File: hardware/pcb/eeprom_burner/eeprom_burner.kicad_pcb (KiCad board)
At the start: 2 copper layers, 68.6 x 53.3 mm, 17 parts, among them J1 Conn_01x08, J2 Conn_01x08, J4 Conn_01x06, P1 Power, P2 Analog, P3 Digital, P4 Digital, P5 CONN_01X01, P6 CONN_01X01, P7 CONN_01X01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

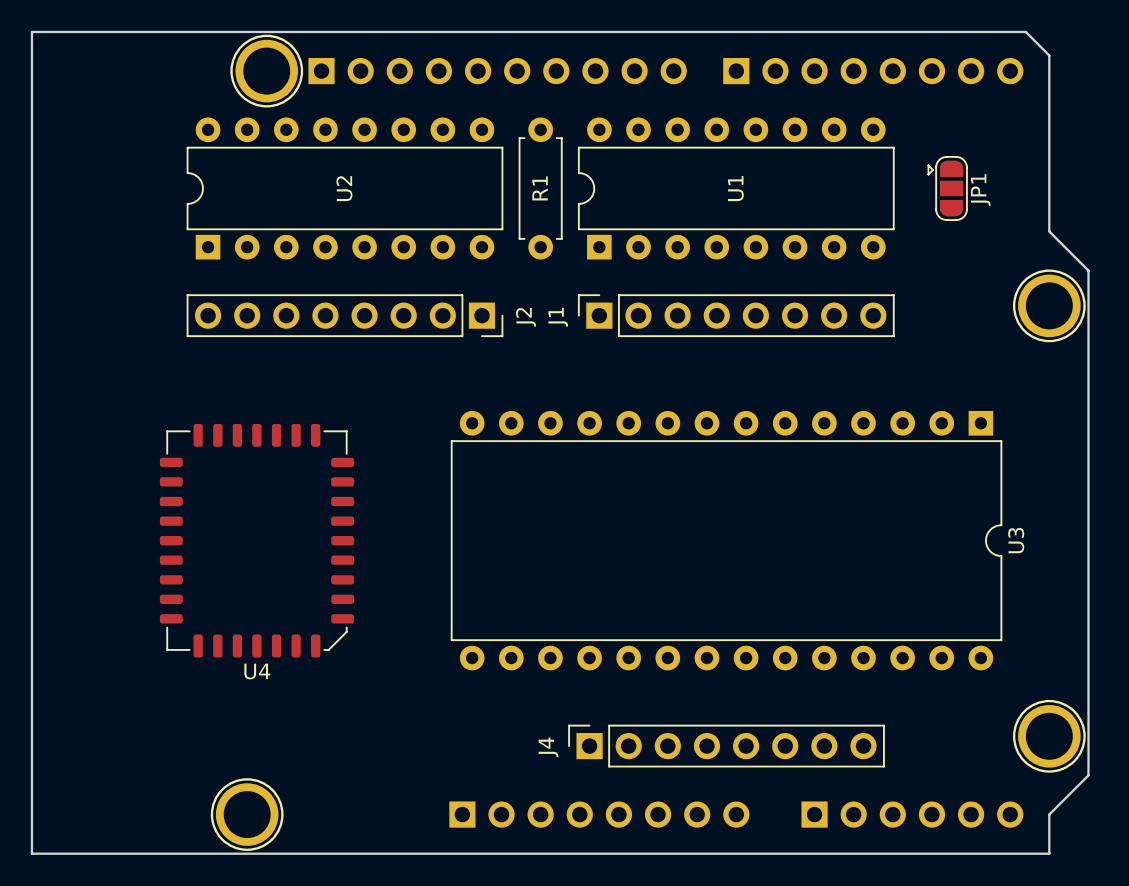
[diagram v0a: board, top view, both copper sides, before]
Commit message: Add decoupling capacitors
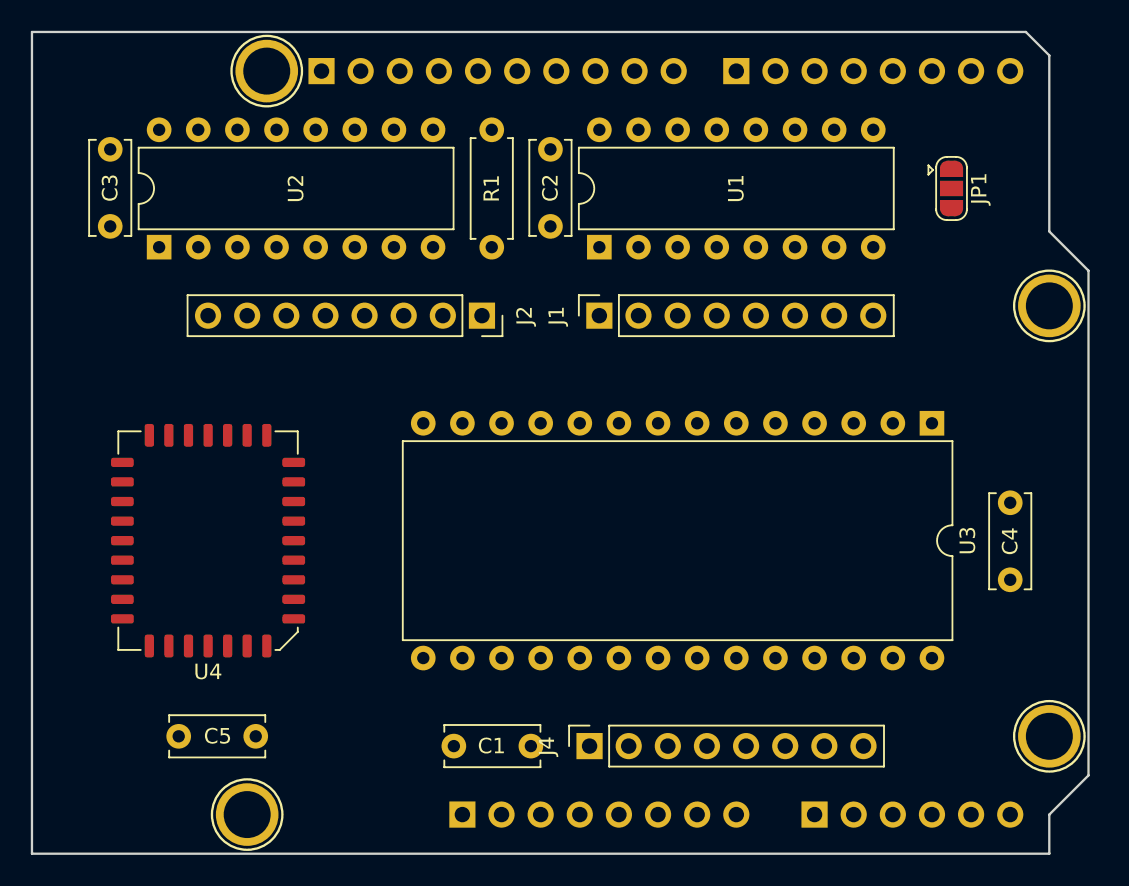
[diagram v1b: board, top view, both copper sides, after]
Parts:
- added C1: 100nF, Capacitor_THT:C_Disc_D6.0mm_W2.5mm_P5.00mm, F.Cu at (143.4, 119.4)
- added C2: 100nF, Capacitor_THT:C_Disc_D6.0mm_W2.5mm_P5.00mm, F.Cu at (144.7, 80.6)
- added C3: 100nF, Capacitor_THT:C_Disc_D6.0mm_W2.5mm_P5.00mm, F.Cu at (116.1, 80.6)
- added C4: 100nF, Capacitor_THT:C_Disc_D6.0mm_W2.5mm_P5.00mm, F.Cu at (174.5, 108.6)
- added C5: 100nF, Capacitor_THT:C_Disc_D6.0mm_W2.5mm_P5.00mm, F.Cu at (120.5, 118.7)
- moved R1 3.18 mm to (140.8, 79.4)
- moved U2 3.17 mm to (119.3, 87.0)
- moved U4 3.17 mm to (122.4, 106.0)
- moved U3 3.17 mm to (169.4, 98.4)

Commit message: Reorder for convinient address access
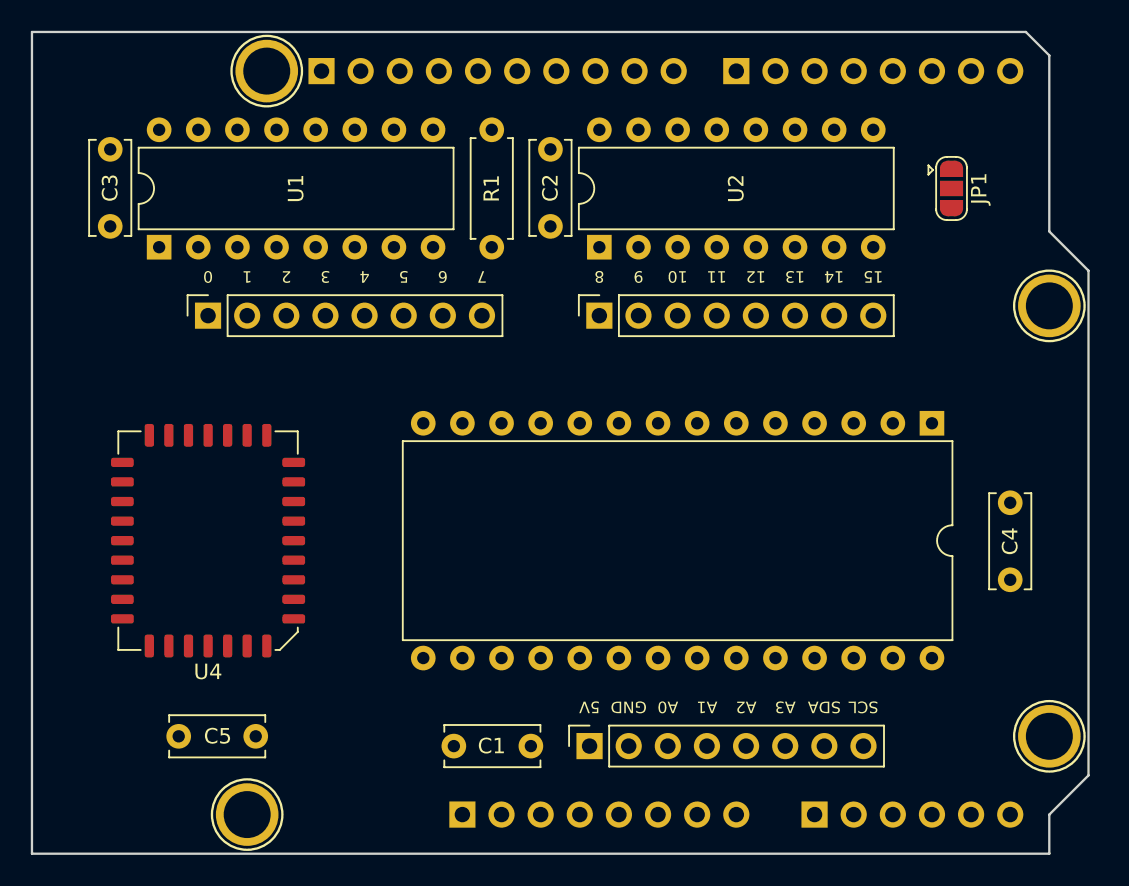
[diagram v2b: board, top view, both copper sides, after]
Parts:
- moved U1 28.6 mm to (119.3, 87.0)
- moved U2 28.6 mm to (147.8, 87.0)
- moved J1 25.4 mm to (122.4, 91.4)
- moved J2 7.62 mm to (147.8, 91.4), turned to 90 degrees
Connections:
- J2 pad 1: A15 -> A8
- J2 pad 2: A14 -> A9
- J2 pad 3: A13 -> A10
- J2 pad 4: A12 -> A11
- J2 pad 5: A11 -> A12
- J2 pad 6: A10 -> A13
- J2 pad 7: A9 -> A14
- J2 pad 8: A8 -> A15
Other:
- board text added: "0"
- board text added: "1"
- board text added: "10"
- board text added: "11"
- board text added: "12"
- board text added: "13"
- board text added: "14"
- board text added: "15"
- board text added: "2"
- board text added: "3"
- board text added: "4"
- board text added: "5"
- board text added: "5V"
- board text added: "6"
- board text added: "7"
- board text added: "8"
- board text added: "9"
- board text added: "A0"
- board text added: "A1"
- board text added: "A2"
- board text added: "A3"
- board text added: "GND"
- board text added: "SCL"
- board text added: "SDA"

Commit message: Add bus connector
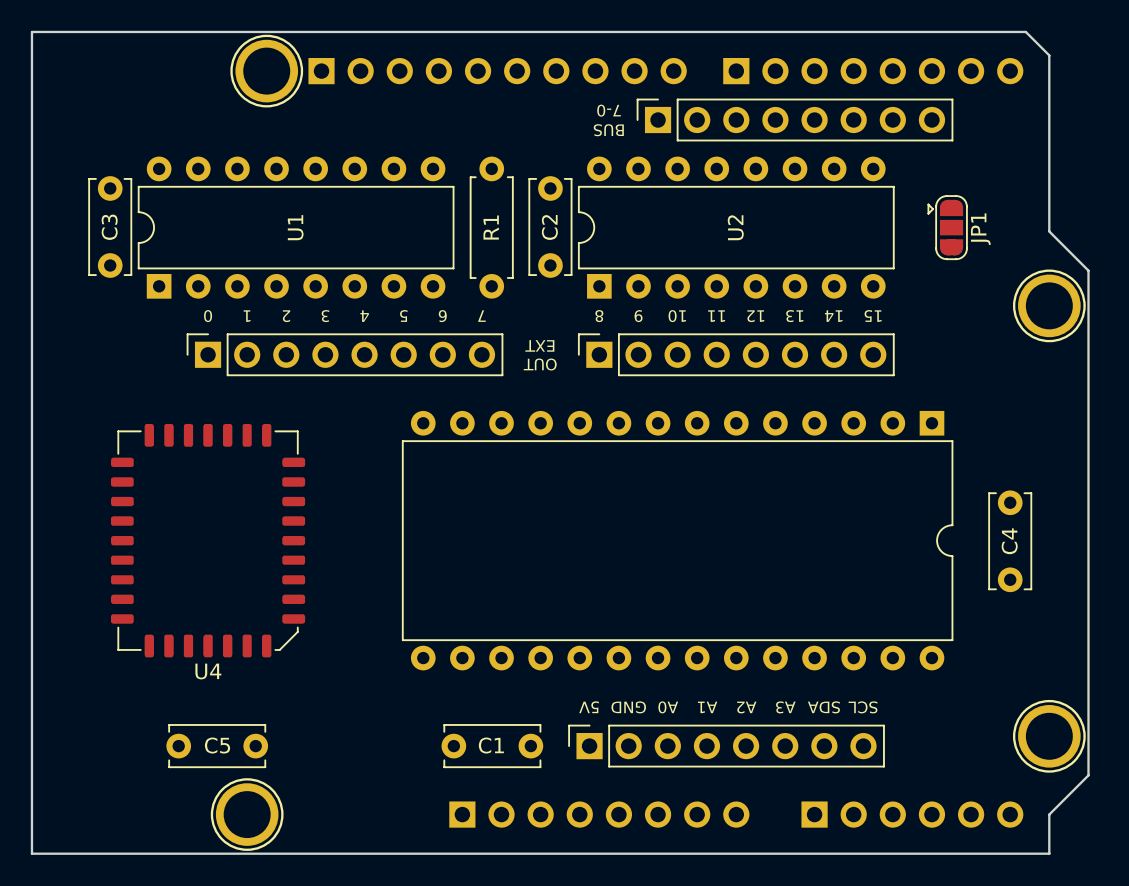
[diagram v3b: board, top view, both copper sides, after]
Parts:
- added J3: Conn_01x08, Connector_PinSocket_2.54mm:PinSocket_1x08_P2.54mm_Vertical, F.Cu at (151.6, 78.7)
- moved C2 2.54 mm to (144.7, 83.2)
- moved C3 2.54 mm to (116.1, 83.2)
- moved J1 2.54 mm to (122.4, 94.0)
- moved J2 2.54 mm to (147.8, 94.0)
- moved R1 2.54 mm to (140.8, 81.9)
- moved JP1 2.54 mm to (170.7, 85.7)
- moved U1 2.54 mm to (119.3, 89.5)
- moved U2 2.54 mm to (147.8, 89.5)
- moved C5 0.63 mm to (120.5, 119.4)
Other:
- board text added: "7-0"
- board text added: "BUS"
- board text added: "OUT EXT"

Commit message: Signature
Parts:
- moved C5 6.35 mm to (126.9, 119.4)
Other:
- board text added: "(c) Velko 2020"
- board text added: "EEPROM writer"
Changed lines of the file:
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@@
   (general
     (thickness 1.6)
-    (drawings 53)
+    (drawings 55)
     (tracks 0)
     (zones 0)
@@
     (descr "Through hole straight pin header, 1x06, 2.54mm pitch, single row")
     (tags "Through hole pin header THT 1x06 2.54mm single row")
-    (fp_text reference P2 (at -2.54 -6.35) (layer B.SilkS)
+    (fp_text reference P2 (at -2.54 -6.35) (layer B.SilkS) hide
       (effects (font (size 1 1) (thickness 0.15)) (justify mirror))
     )
@@
     (descr "Through hole straight pin header, 1x08, 2.54mm pitch, single row")
     (tags "Through hole pin header THT 1x08 2.54mm single row")
-    (fp_text reference P1 (at -2.54 -8.89) (layer B.SilkS)
+    (fp_text reference P1 (at -2.54 -8.89) (layer B.SilkS) hide
       (effects (font (size 1 1) (thickness 0.15)) (justify mirror))
     )
@@
     (descr "Through hole straight pin header, 1x08, 2.54mm pitch, single row")
     (tags "Through hole pin header THT 1x08 2.54mm single row")
-    (fp_text reference P4 (at 2.54 -9.525 180) (layer B.SilkS)
+    (fp_text reference P4 (at 2.54 -9.525 180) (layer B.SilkS) hide
       (effects (font (size 1 1) (thickness 0.15)) (justify mirror))
     )
@@
     (descr "Through hole straight pin header, 1x10, 2.54mm pitch, single row")
     (tags "Through hole pin header THT 1x10 2.54mm single row")
-    (fp_text reference P3 (at 2.54 -12.319 180) (layer B.SilkS)
+    (fp_text reference P3 (at 2.54 -12.319 180) (layer B.SilkS) hide
       (effects (font (size 1 1) (thickness 0.15)) (justify mirror))
     )
@@
   )
   (module Capacitor_THT:C_Disc_D6.0mm_W2.5mm_P5.00mm (layer F.Cu)
-    (at 120.523 119.38)
+    (at 126.873 119.38)
     (descr "C, Disc series, Radial, pin pitch=5.00mm, , diameter*width=6*2.5mm^2, Capacitor, http://cdn-reichelt.de/documents/datenblatt/B300/DS_KERKO_TC.pdf")
     (tags "C Disc series Radial pin pitch 5.00mm  diameter 6mm width 2.5mm Capacitor")
@@
     )
   )
+  (gr_text "EEPROM\nwriter" (at 117.983 120.65 180) (layer F.SilkS)
+    (effects (font (size 1.5 1.5) (thickness 0.3)))
+  )
+  (gr_text "(c) Velko 2020" (at 137.033 78.74 180) (layer F.SilkS)
+    (effects (font (size 1.5 1.5) (thickness 0.3)))
+  )
   (gr_text "OUT\nEXT" (at 144.018 93.98 180) (layer F.SilkS)

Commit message: Moved signatures
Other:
- board text added: "Velko 2020"
- board text removed: "(c) Velko 2020"
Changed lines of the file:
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@@
     )
   )
-  (gr_text "EEPROM\nwriter" (at 117.983 120.65 180) (layer F.SilkS)
+  (gr_text "EEPROM\nwriter" (at 116.713 121.285 180) (layer F.SilkS)
     (effects (font (size 1.5 1.5) (thickness 0.3)))
   )
-  (gr_text "(c) Velko 2020" (at 137.033 78.74 180) (layer F.SilkS)
+  (gr_text "Velko\n2020" (at 117.983 77.47 180) (layer F.SilkS)
     (effects (font (size 1.5 1.5) (thickness 0.3)))
   )

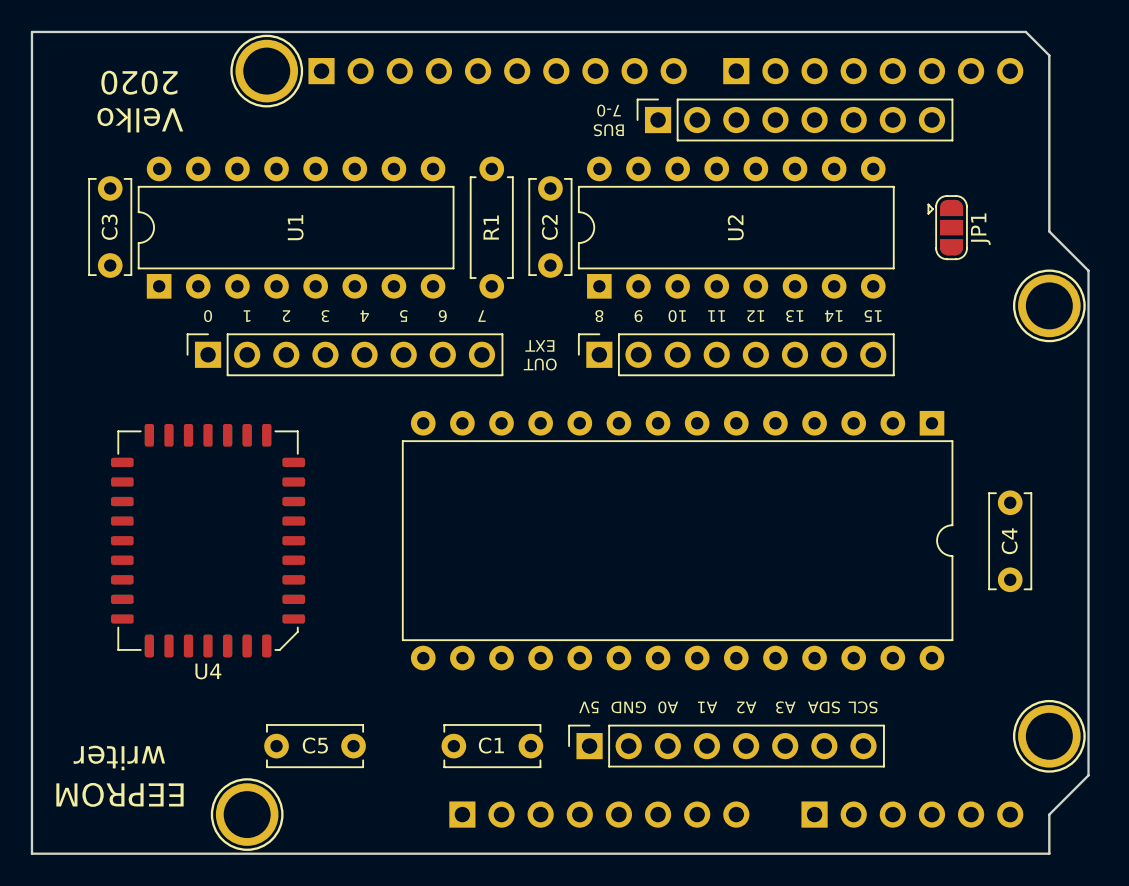
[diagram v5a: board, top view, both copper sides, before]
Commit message: Add ground plane
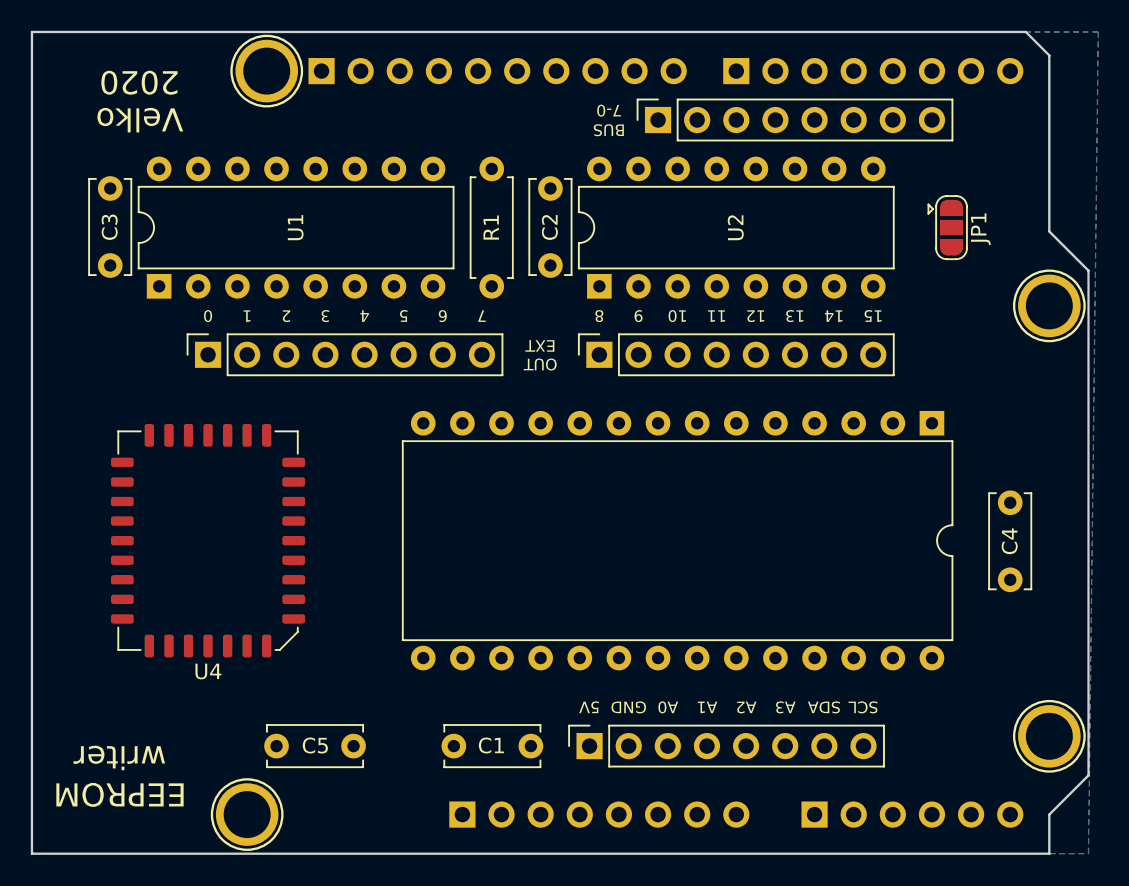
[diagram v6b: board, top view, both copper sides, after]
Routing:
- added copper zone on B.Cu, net GND
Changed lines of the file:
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@@
   (gr_line (start 120.523 82.55) (end 120.523 93.98) (angle 90) (layer Dwgs.User) (width 0.15))
   (gr_line (start 104.648 82.55) (end 120.523 82.55) (angle 90) (layer Dwgs.User) (width 0.15))
+  (zone (net 2) (net_name GND) (layer B.Cu) (hatch edge 0.508)
+    (connect_pads (clearance 0.508))
+    (min_thickness 0.254)
+    (fill yes (arc_segments 16) (thermal_gap 0.508) (thermal_bridge_width 0.508))
+    (polygon
+      (pts
+        (xy 110.998 73.025) (xy 110.998 126.365) (xy 179.578 126.365) (xy 180.213 73.025)
+      )
+    )
+  )
 )

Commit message: Import autorouted PCB
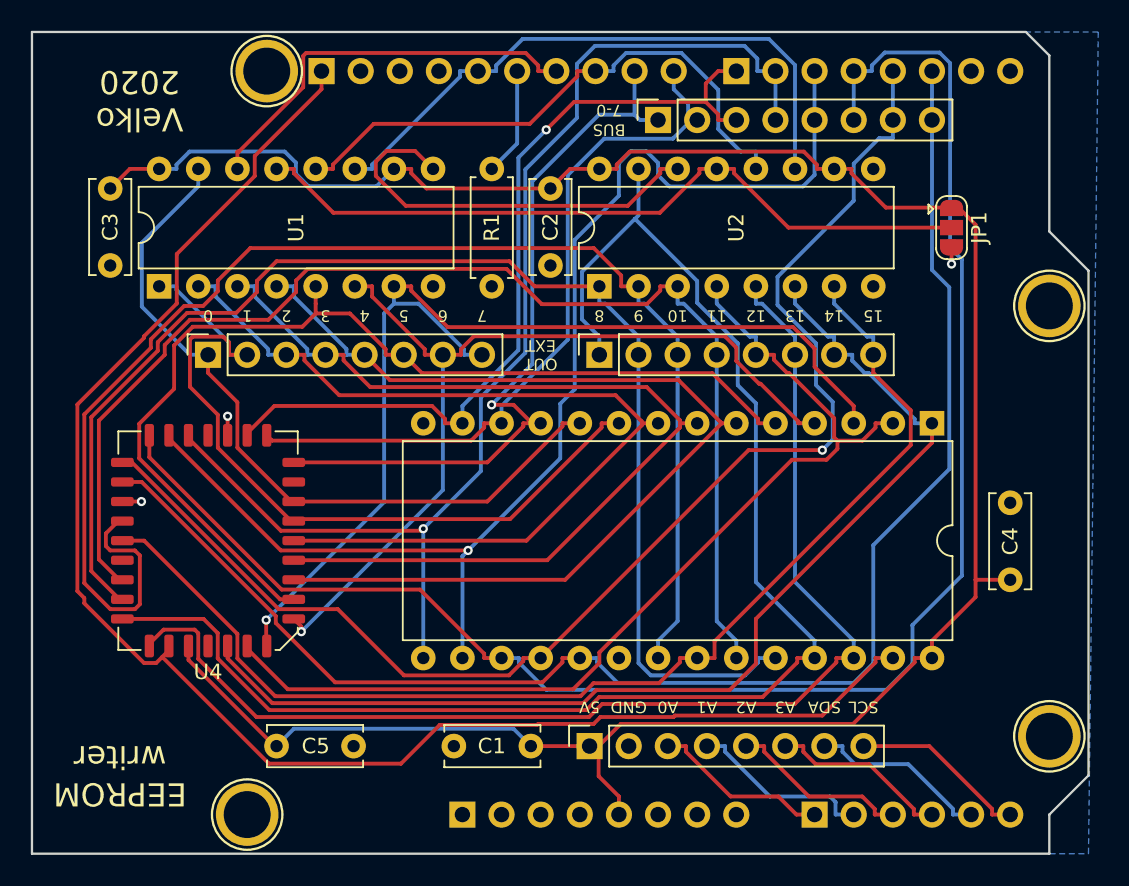
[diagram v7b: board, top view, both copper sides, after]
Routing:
- net +5V: track 0.00 -> 154.8 mm
- net D5: track 0.00 -> 109.3 mm
- net ~WE~: track 0.00 -> 102.3 mm
- net D7: track 0.00 -> 97.5 mm
- net A8: track 0.00 -> 97.3 mm
- net A10: track 0.00 -> 91.8 mm
- net D6: track 0.00 -> 87.3 mm, vias 0 -> 1
- net A9: track 0.00 -> 87.0 mm
- net A11: track 0.00 -> 81.1 mm
- net D4: track 0.00 -> 80.5 mm, vias 0 -> 1
- net D3: track 0.00 -> 78.4 mm, vias 0 -> 1
- net A13: track 0.00 -> 78.3 mm
- net A15: track 0.00 -> 76.4 mm
- net A14: track 0.00 -> 72.0 mm
- net A7: track 0.00 -> 69.1 mm, vias 0 -> 1
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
